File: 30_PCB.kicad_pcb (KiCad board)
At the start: 4 copper layers, 70 x 55 mm, 36 parts, among them J1 IPM-165-Radar, J10 TEST_VCC, J11 TEST_OUT, J2 TEST_AMPLIN, J3 TEST_AMPL1_OUT, J4 TEST_AMPL2_OUT, J6 TEST_GNDD, J7 TEST_GNDD, J8 TEST_GNDA, J9 TEST_GNDA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

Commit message: PCB R0.5/Schema R0.6
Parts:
- added R12: 1k, Resistor_SMD:R_1206_3216Metric_Pad1.42x1.75mm_HandSolder, F.Cu at (140.5, 75.7)
- C1, C2, C5: footprint Capacitor_THT:C_Radial_D5.0mm_H11.0mm_P2.00mm -> Capacitor_THT:CP_Radial_D5.0mm_P2.00mm
- C4: footprint Capacitor_THT:C_Rect_L7.2mm_W3.5mm_P5.00mm_FKS2_FKP2_MKS2_MKP2 -> Capacitor_THT:C_Rect_L7.2mm_W2.5mm_P5.00mm_FKS2_FKP2_MKS2_MKP2
- C6: footprint Capacitor_THT:C_Rect_L7.2mm_W5.5mm_P5.00mm_FKS2_FKP2_MKS2_MKP2 -> Capacitor_THT:C_Rect_L7.2mm_W4.5mm_P5.00mm_FKS2_FKP2_MKS2_MKP2
- D1, D2, D3, D4: footprint Diode_SMD:D_1206_3216Metric -> Diode_SMD:D_1206_3216Metric_Pad1.42x1.75mm_HandSolder
- R10, R11, R7, R9: footprint Resistor_SMD:R_1206_3216Metric -> Resistor_SMD:R_1206_3216Metric_Pad1.42x1.75mm_HandSolder
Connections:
- U1 pad 4: (no net) -> GNDA
- U1 pad 8: (no net) -> VCC
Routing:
- net VCC: track 19.2 -> 10.2 mm
- net Net-(R12-Pad2): track 43.3 -> 51.6 mm
- net Net-(C6-Pad2): track 17.1 -> 15.6 mm
- net /AMPLFR_IN: track 11.8 -> 12.5 mm
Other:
- board text added: "24 GHz Radar Motion Detector PCB Rev: R0.5/Schema Rev: R0.6 Swagat Panda (766473) Date:15/05/2020"
- board text added: "VCC IPM-165"
- board text removed: "24 GHz Radar Moton Detector PCB Rev: R0.4/Schema Rev: R0.5 Swagat Panda (766473) Date:15/05/2020"

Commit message: PCB R0.6/Schema R0.7--most likely final version
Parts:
- R1, R2, R3, R4, R5, R6, R8: footprint Resistor_THT:R_Axial_DIN0204_L3.6mm_D1.6mm_P7.62mm_Horizontal -> Resistor_THT:R_Axial_DIN0207_L6.3mm_D2.5mm_P7.62mm_Horizontal
- moved G*** 0.75 mm to (121.7, 88.6)
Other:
- board text added: "24 GHz Radar Motion Detector PCB Rev: R0.6/Schema Rev: R0.7 Swagat Panda (766473) Date:15/05/2020"
- board text removed: "24 GHz Radar Motion Detector PCB Rev: R0.5/Schema Rev: R0.6 Swagat Panda (766473) Date:15/05/2020"

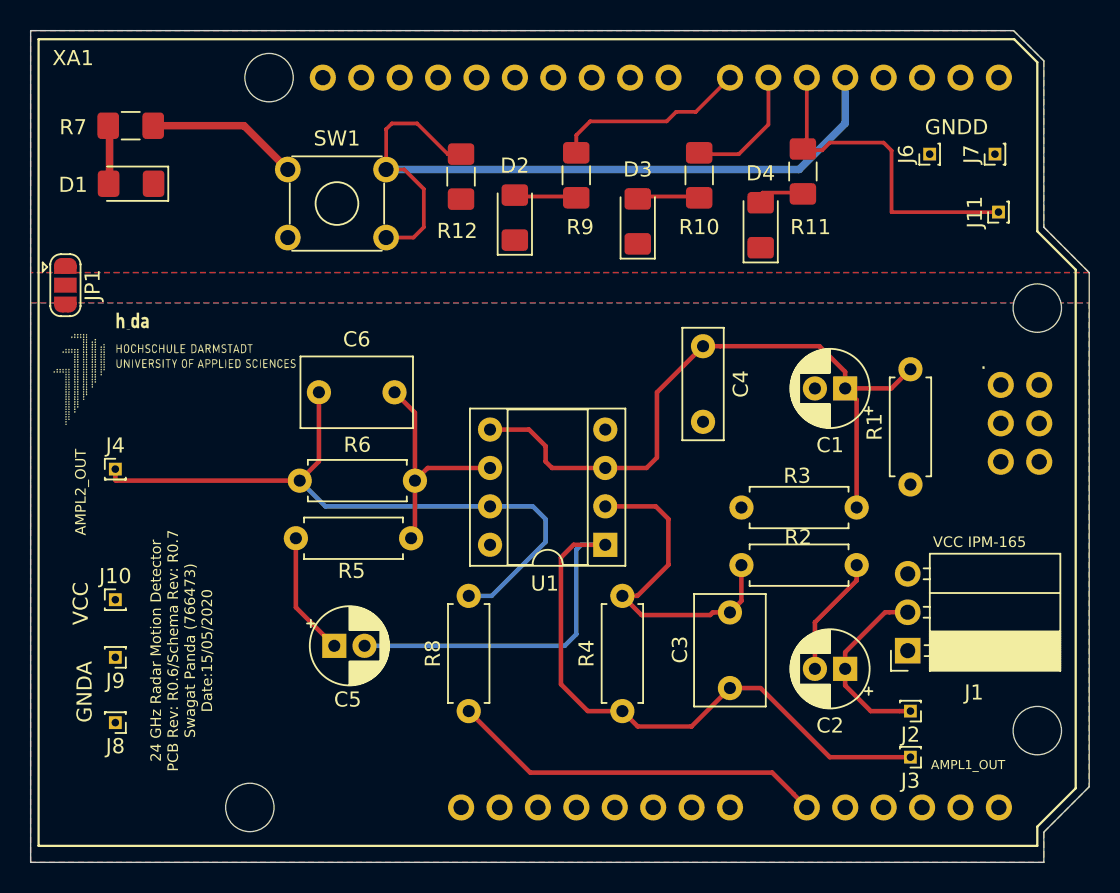
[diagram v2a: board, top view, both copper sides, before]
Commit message: PCB R0.7/Schema R0.8 -- Descriptions added,minor modification,Final Version
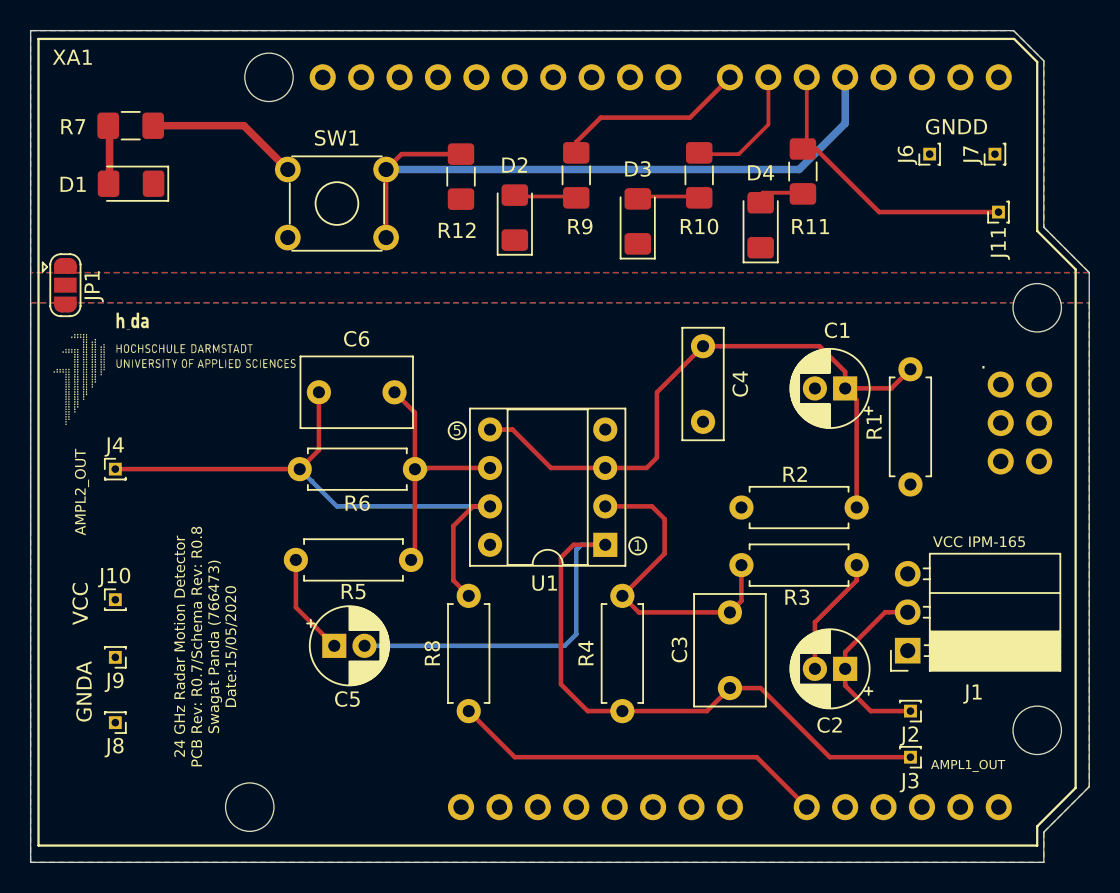
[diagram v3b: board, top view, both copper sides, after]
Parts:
- moved R5 1.43 mm to (137.2, 101.0)
- moved R6 0.76 mm to (129.8, 95.0)
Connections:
- net Net-(JP1-Pad2) renamed GND
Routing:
- net Net-(R12-Pad2): track 51.6 -> 45.4 mm
- net Net-(C6-Pad1): track 44.7 -> 39.4 mm
- net Net-(J11-Pad1): track 22.3 -> 19.6 mm
- net Net-(C6-Pad2): track 15.6 -> 17.8 mm
- net Net-(C5-Pad1): track 8.16 -> 6.73 mm
- net Net-(C3-Pad2): track 22.6 -> 21.5 mm
- net Net-(C3-Pad1): track 60.8 -> 60.0 mm
- net Net-(C1-Pad1): track 45.8 -> 45.2 mm
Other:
- board text added: "1"
- board text added: "24 GHz Radar Motion Detector PCB Rev: R0.7/Schema Rev: R0.8 Swagat Panda (766473) Date:15/05/2020"
- board text added: "5"
- board text removed: "24 GHz Radar Motion Detector PCB Rev: R0.6/Schema Rev: R0.7 Swagat Panda (766473) Date:15/05/2020"
